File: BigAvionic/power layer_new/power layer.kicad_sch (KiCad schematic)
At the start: 56 parts, among them J1 Conn_01x04, J2 Conn_01x04, J3 Conn_01x04, J4 Conn_01x04, J5 Conn_01x02, J6 USB_C_Receptacle_USB2.0_16P, Q1 TSM3481CX6 RFG, Q2 TSM3481CX6 RFG, U2 LD1117S33TR_SOT223, U3 LTC4412xS6, U4 TPS54538RQFR

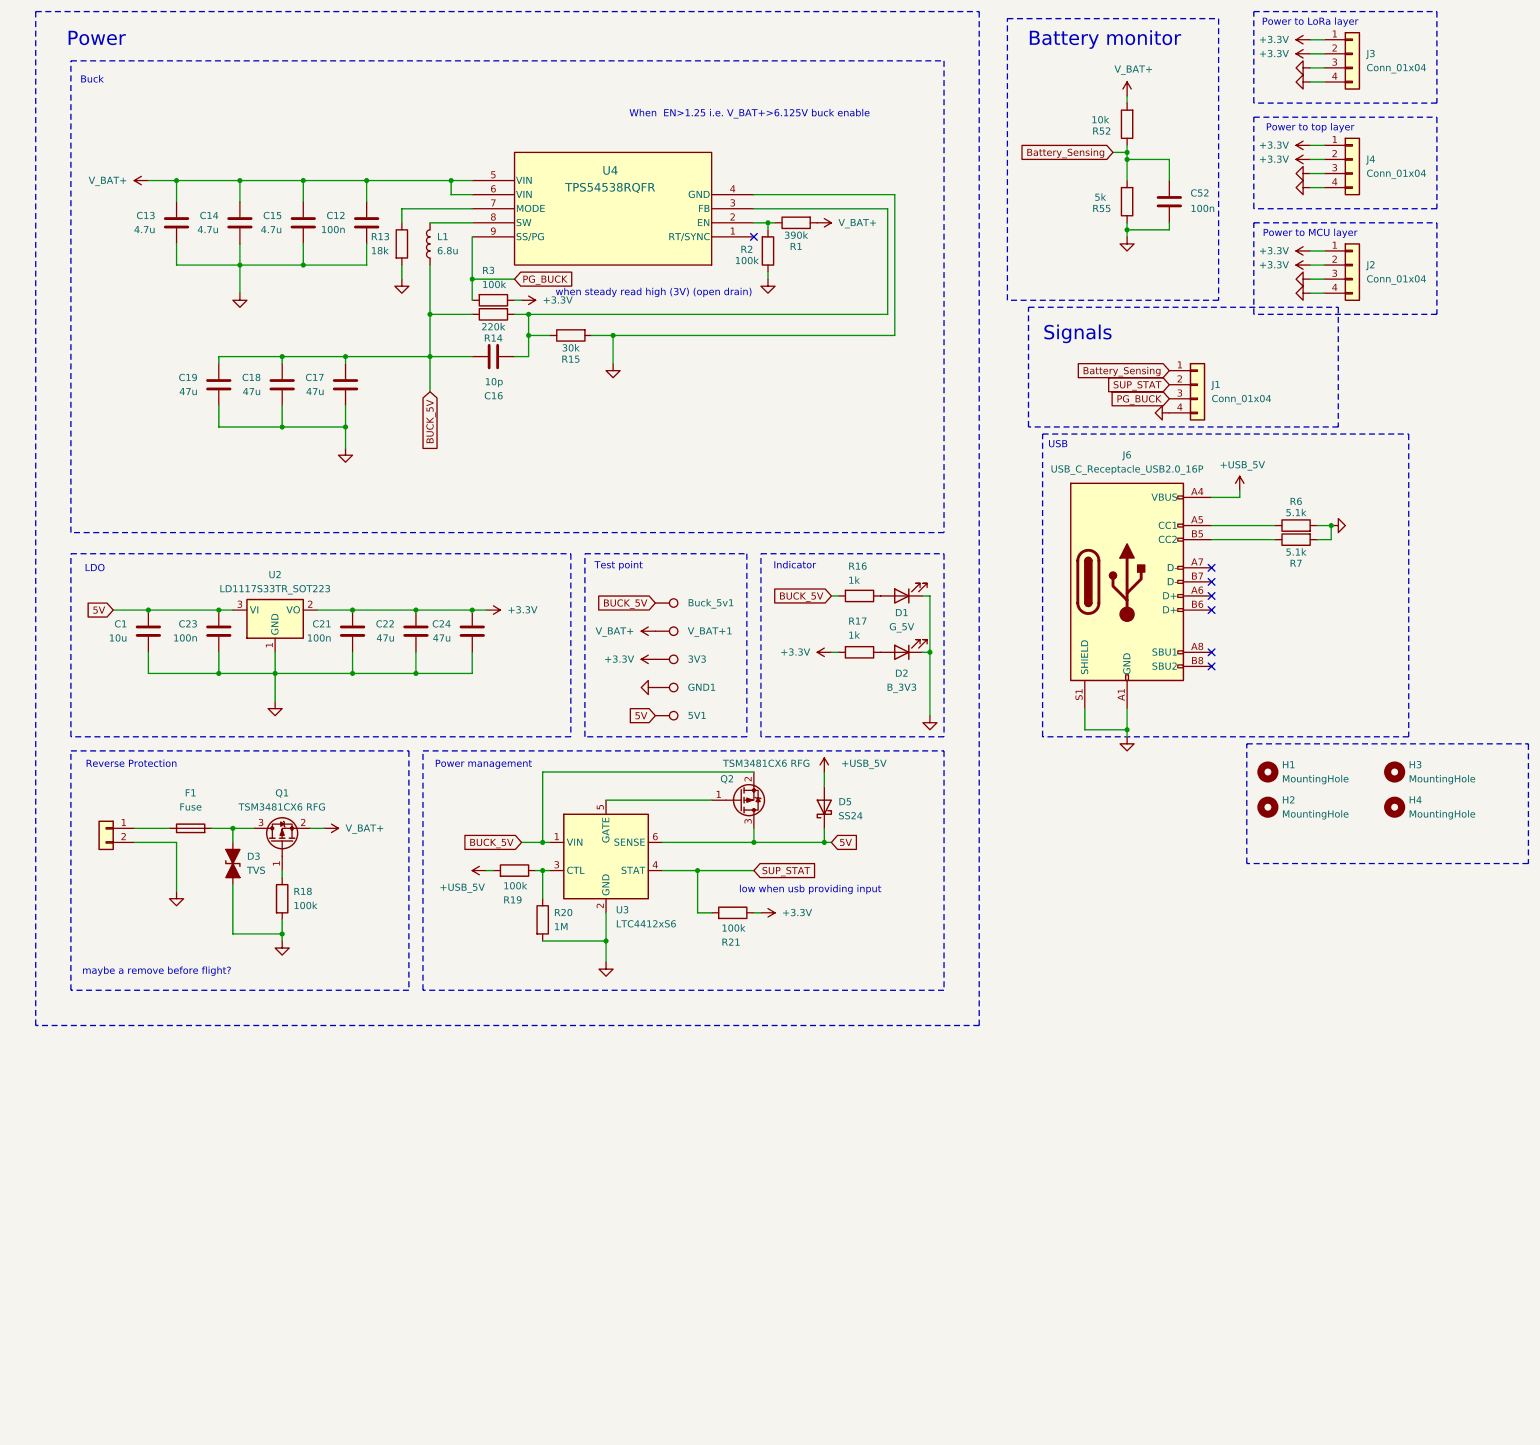
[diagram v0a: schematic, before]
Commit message: change GS MOS
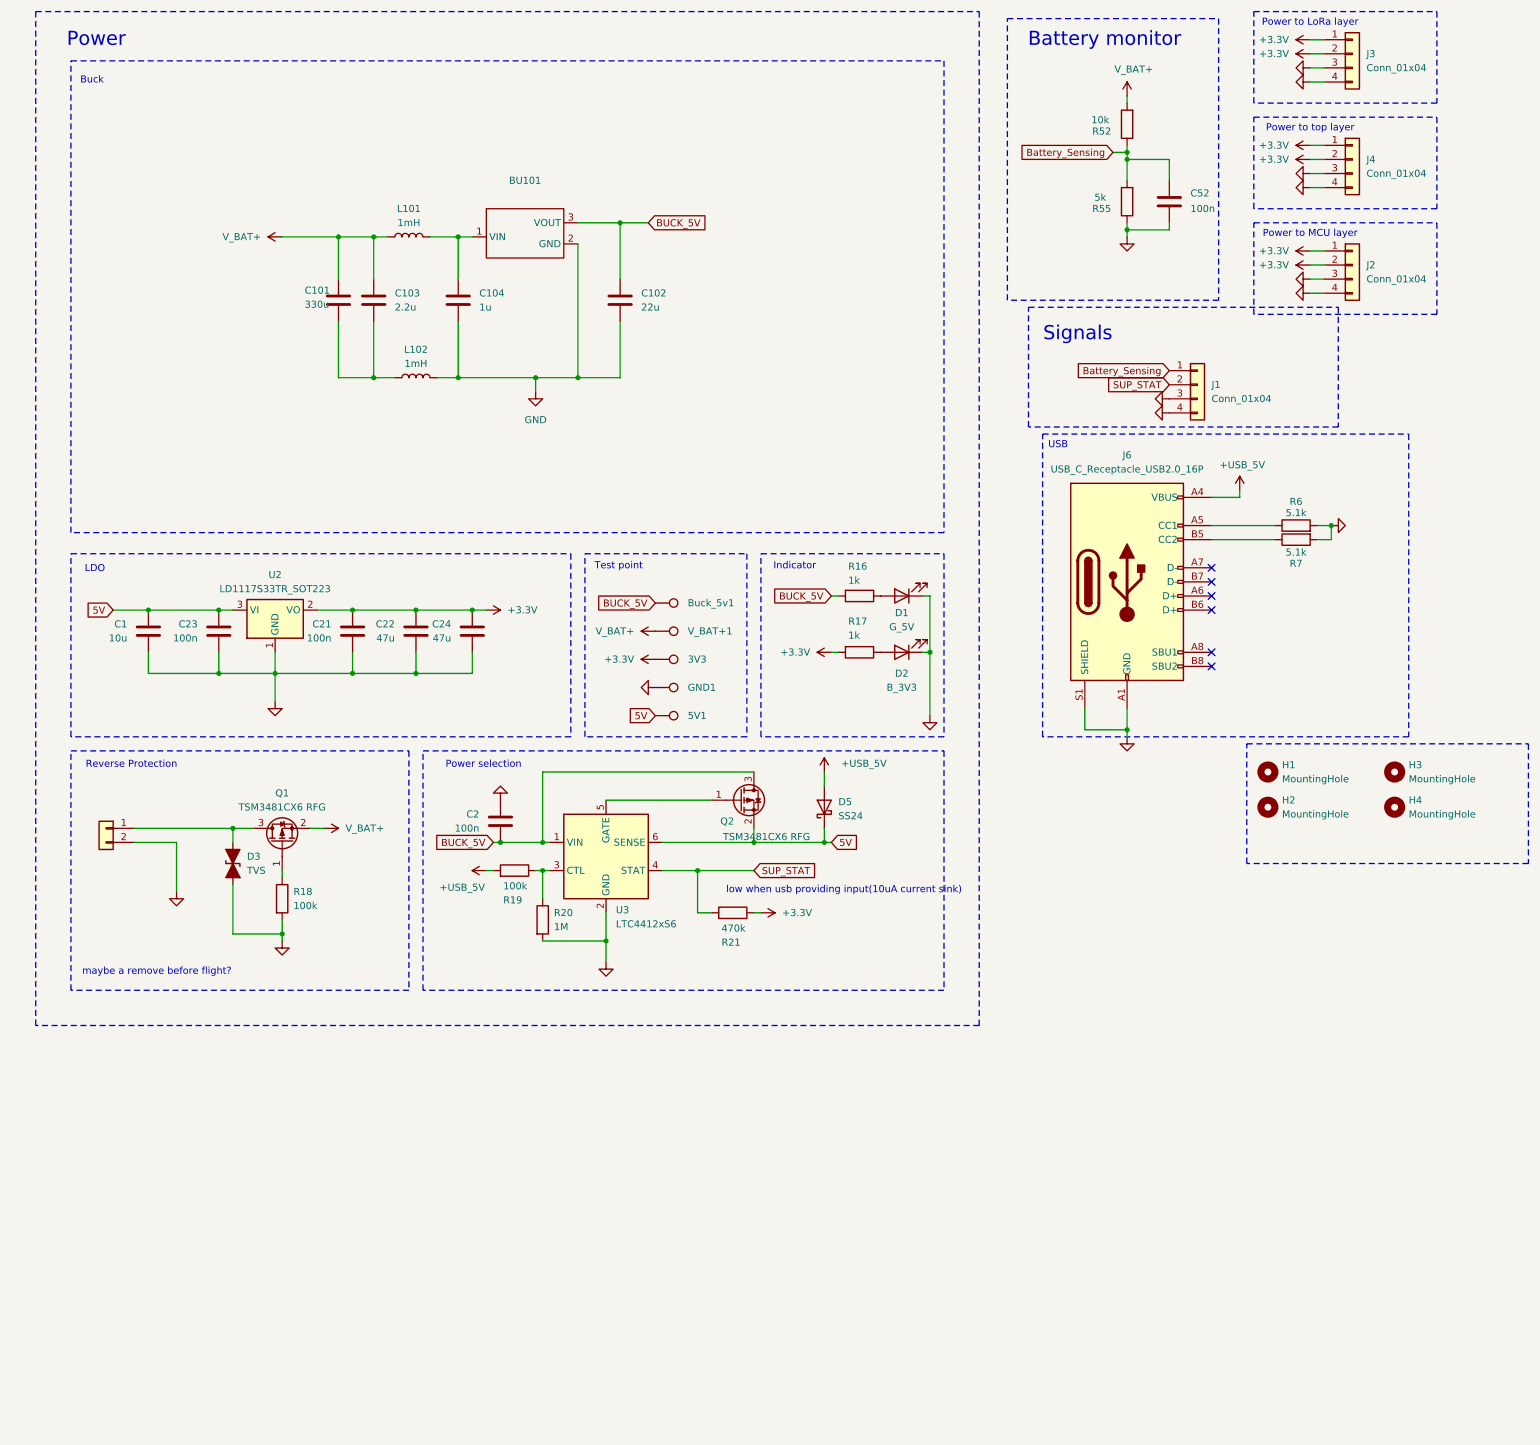
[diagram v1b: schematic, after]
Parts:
- removed C12: 100n, Capacitor_SMD:C_0603_1608Metric_Pad1.08x0.95mm_HandSolder, symbol Device:C
- removed C13, C14, C15: 4.7u, Capacitor_SMD:C_1206_3216Metric_Pad1.33x1.80mm_HandSolder, symbol Device:C
- removed C16: 10p, Capacitor_SMD:C_0402_1005Metric_Pad0.74x0.62mm_HandSolder, symbol Device:C
- removed C17, C18, C19: 47u, Capacitor_SMD:C_1206_3216Metric_Pad1.33x1.80mm_HandSolder, symbol Device:C
- removed F1: Fuse, Fuse:Fuse_0805_2012Metric_Pad1.15x1.40mm_HandSolder, symbol Device:Fuse
- removed L1: 6.8u, Inductor_SMD:L_7.3x7.3_H3.5, symbol Device:L
- removed R1: 390k, Capacitor_SMD:C_0603_1608Metric_Pad1.08x0.95mm_HandSolder, symbol Device:R
- removed R13: 18k, Capacitor_SMD:C_0603_1608Metric_Pad1.08x0.95mm_HandSolder, symbol Device:R
- removed R14: 220k, Capacitor_SMD:C_0603_1608Metric_Pad1.08x0.95mm_HandSolder, symbol Device:R
- removed R15: 30k, Capacitor_SMD:C_0603_1608Metric_Pad1.08x0.95mm_HandSolder, symbol Device:R
- removed R2, R3: 100k, Capacitor_SMD:C_0603_1608Metric_Pad1.08x0.95mm_HandSolder, symbol Device:R
- removed U4: TPS54538RQFR, Tony:VQFN-HR9_RQF_TEX(TPS54538), symbol Small_av_tony_lib:TPS54538RQFR
- added BU101: ~, Tony:CONV_R-78K5.0-2.0L, symbol New_Library_0:BK
- added C101: 330u, Capacitor_SMD:C_0805_2012Metric_Pad1.18x1.45mm_HandSolder, symbol Device:C
- added C102: 22u, Capacitor_SMD:C_0805_2012Metric_Pad1.18x1.45mm_HandSolder, symbol Device:C
- added C103: 2.2u, Capacitor_SMD:C_0805_2012Metric_Pad1.18x1.45mm_HandSolder, symbol Device:C
- added C104: 1u, Capacitor_SMD:C_0805_2012Metric_Pad1.18x1.45mm_HandSolder, symbol Device:C
- added C2: 100n, Capacitor_SMD:C_0805_2012Metric_Pad1.18x1.45mm_HandSolder, symbol Device:C
- added L101, L102: 1mH, Inductor_SMD:L_0805_2012Metric_Pad1.05x1.20mm_HandSolder, symbol Device:L
- R21: value 100k -> 470k
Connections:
- net PG_BUCK is gone; now on net GND: J1.3 (Pin_3)
- net 5V: now also Q2.2 (S); no longer Q2.3 (D)
- net BUCK_5V: now also Q2.3 (D), BU101.3 (VOUT), C102.1, C2.2; no longer Q2.2 (S)
- net GND: now also BU101.2 (GND), C102.2, C104.2, C2.1, L102.2
- net V_BAT+: now also C101.1, C103.1, L101.1
- net at J5.1 (Pin_1): now also D3.2 (A2), Q1.3 (D)
- new net: BU101.1 (VIN), C104.1, L101.2
- new net: C101.2, C103.2, L102.1
- no-connect marks 7 -> 6
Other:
- note added: "Power selection"
- note added: "low when usb providing input(10uA current sink)"
- note removed: "Power management"
- note removed: "When EN>1.25 i.e. V_BAT+>6.125V buck enable"
- note removed: "low when usb providing input"
- note removed: "when steady read high (3V) (open drain)"

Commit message: power layer finished
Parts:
- removed C104: 1u, Capacitor_SMD:C_0805_2012Metric_Pad1.18x1.45mm_HandSolder, symbol Device:C
- removed L101, L102: 1mH, Inductor_SMD:L_0805_2012Metric_Pad1.05x1.20mm_HandSolder, symbol Device:L
- removed Q1, Q2: TSM3481CX6 RFG, Package_TO_SOT_SMD:SOT-23, symbol Transistor_FET:IRLML6402
- added 3V3_LORA1: TestPoint, TestPoint:TestPoint_Pad_D1.0mm, symbol Connector:TestPoint
- added BU2: R-78K3.3-2.0L, Tony:CONV_R-78K5.0-2.0L, symbol New_Library_0:BK
- added C12, C3, C6: 22u, Capacitor_SMD:C_1210_3225Metric_Pad1.33x2.70mm_HandSolder, symbol Device:C
- added C13: 47u, Capacitor_SMD:C_1210_3225Metric_Pad1.33x2.70mm_HandSolder, symbol Device:C
- added C15: 100n, Capacitor_SMD:C_0805_2012Metric_Pad1.18x1.45mm_HandSolder, symbol Device:C
- added C_Damping1, C_Damping2: 22u, Capacitor_Tantalum_SMD:CP_EIA-3528-21_Kemet-B_HandSolder, symbol Device:C
- added D5: G_3V3, LED_SMD:LED_0805_2012Metric_Pad1.15x1.40mm_HandSolder, symbol Device:LED
- added L1, L2: 4.7uH, Inductor_SMD:L_APV_ANR4020, symbol Device:L
- added Q1, Q2: AO3401A, Package_TO_SOT_SMD:SOT-23, symbol Transistor_FET:AO3401A
- added R11: 470, Resistor_SMD:R_0805_2012Metric_Pad1.20x1.40mm_HandSolder, symbol Device:R
- 5V1, GND1: footprint TestPoint:TestPoint_Pad_1.0x1.0mm -> TestPoint:TestPoint_Pad_D1.0mm
- BU1: renamed from BU101; value ~ -> R-78K5.0-2.0L
- C1: footprint Capacitor_SMD:C_0805_2012Metric_Pad1.18x1.45mm_HandSolder -> Capacitor_SMD:C_1210_3225Metric_Pad1.33x2.70mm_HandSolder
- C11: renamed from C102; footprint Capacitor_SMD:C_0805_2012Metric_Pad1.18x1.45mm_HandSolder -> Capacitor_SMD:C_1210_3225Metric_Pad1.33x2.70mm_HandSolder
- C2: renamed from C101; value 330u -> 22u; footprint Capacitor_SMD:C_0805_2012Metric_Pad1.18x1.45mm_HandSolder -> Capacitor_SMD:C_1210_3225Metric_Pad1.33x2.70mm_HandSolder
- C5: renamed from C103; value 2.2u -> 22u; footprint Capacitor_SMD:C_0805_2012Metric_Pad1.18x1.45mm_HandSolder -> Capacitor_SMD:C_1210_3225Metric_Pad1.33x2.70mm_HandSolder
- C8: renamed from C22; footprint Capacitor_SMD:C_1206_3216Metric_Pad1.33x1.80mm_HandSolder -> Capacitor_SMD:C_1210_3225Metric_Pad1.33x2.70mm_HandSolder
- C9: renamed from C24; footprint Capacitor_SMD:C_1206_3216Metric_Pad1.33x1.80mm_HandSolder -> Capacitor_SMD:C_1210_3225Metric_Pad1.33x2.70mm_HandSolder
- D1: renamed from D3; footprint LED_SMD:LED_0805_2012Metric_Pad1.15x1.40mm_HandSolder -> Diode_SMD:D_SMA
- D4: renamed from D2; value B_3V3 -> G_3V3
- R1: renamed from R18; footprint Capacitor_SMD:C_0603_1608Metric_Pad1.08x0.95mm_HandSolder -> Resistor_SMD:R_0805_2012Metric_Pad1.20x1.40mm_HandSolder
- R2: renamed from R19; footprint Capacitor_SMD:C_0603_1608Metric_Pad1.08x0.95mm_HandSolder -> Resistor_SMD:R_0805_2012Metric_Pad1.20x1.40mm_HandSolder
- R3: renamed from R20; footprint Capacitor_SMD:C_0603_1608Metric_Pad1.08x0.95mm_HandSolder -> Resistor_SMD:R_0805_2012Metric_Pad1.20x1.40mm_HandSolder
- R4: renamed from R21; footprint Capacitor_SMD:C_0603_1608Metric_Pad1.08x0.95mm_HandSolder -> Resistor_SMD:R_0805_2012Metric_Pad1.20x1.40mm_HandSolder
- R5: renamed from R16; footprint Capacitor_SMD:C_0603_1608Metric_Pad1.08x0.95mm_HandSolder -> Resistor_SMD:R_0805_2012Metric_Pad1.20x1.40mm_HandSolder
- R6: renamed from R17; value 1k -> 470; footprint Capacitor_SMD:C_0603_1608Metric_Pad1.08x0.95mm_HandSolder -> Resistor_SMD:R_0805_2012Metric_Pad1.20x1.40mm_HandSolder
- R7: renamed from R52; footprint Capacitor_SMD:C_0603_1608Metric_Pad1.08x0.95mm_HandSolder -> Resistor_SMD:R_0805_2012Metric_Pad1.20x1.40mm_HandSolder
- R8: renamed from R55; footprint Capacitor_SMD:C_0603_1608Metric_Pad1.08x0.95mm_HandSolder -> Resistor_SMD:R_0805_2012Metric_Pad1.20x1.40mm_HandSolder
- renumbered 3V3 to 3V3_1, C2 to C10, C52 to C14, C23 to C4, C21 to C7, D5 to D2, D1 to D3, J5 to J1, J6 to J2, J1 to J3, J3 to J4, J4 to J5, J2 to J6, R7 to R10, R6 to R9, U2 to U1, U3 to U2
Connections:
- net +3.3V: no longer J6.1 (Pin_1), J6.2 (Pin_2)
- net 5V: now also R5.2, C13.2, C3.1, L2.1, Q2.2 (S)
- net BUCK_5V: now also Q2.3 (D); no longer R5.2
- net GND: now also C2.2, C5.2, BU2.2 (GND), C12.2, C13.1, C15.2, C3.2, C6.2, C_Damping1.2, C_Damping2.2, D5.1 (K)
- net V_BAT+: now also L1.1, Q1.2 (S); no longer C5.1
- net at BU1.1 (VIN): now also C5.1, C_Damping2.1, L1.2
- net at U2.5 (GATE): now also Q2.1 (G)
- net at D1.2 (A2), J1.1 (Pin_1): now also Q1.3 (D)
- net at R1.1: now also Q1.1 (G)
- new net: D5.2 (A), R11.1
- new net: BU2.1 (VIN), C6.1, C_Damping1.1, L2.2
- new net +3.3V_LoRa: 3V3_LORA1.1, BU2.3 (VOUT), C12.1, C15.1, J6.1 (Pin_1), J6.2 (Pin_2), R11.2
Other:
- note added: "Buck->5V"
- note added: "buck LoRa->3V3"
- note added: "maybe a pi filter in oupput also"
- note removed: "Buck"
- moved on the sheet: 3V3_1, 5V1, BU1, Buck_5v1, C1, C10, C11, C2, C4, C5, C7, C8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

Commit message: version for v1 production
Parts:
- R11, R6: value 470 -> 100
- R5: value 1k -> 330
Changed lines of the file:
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@@
 			)
 		)
-		(property "Value" "1k"
+		(property "Value" "330"
 			(at 159.258 161.036 90)
 			(effects
@@
 			)
 		)
-		(property "Value" "470"
+		(property "Value" "100"
 			(at 157.988 152.146 90)
 			(effects
@@
 			)
 		)
-		(property "Value" "470"
+		(property "Value" "100"
 			(at 159.258 170.942 90)
 			(effects

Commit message: update step
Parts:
- D3: value G_5V -> ~
- D4, D5: value G_3V3 -> ~
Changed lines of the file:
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@@
 			)
 		)
-		(property "Value" "G_5V"
+		(property "Value" "~"
 			(at 168.91 169.418 0)
 			(effects
@@
 			)
 		)
-		(property "Value" "G_3V3"
+		(property "Value" "~"
 			(at 168.91 180.34 0)
 			(effects
@@
 			)
 		)
-		(property "Value" "G_3V3"
+		(property "Value" "~"
 			(at 168.91 161.29 0)
 			(effects
